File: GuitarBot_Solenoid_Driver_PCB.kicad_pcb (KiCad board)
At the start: 2 copper layers, 68 parts, among them J3V3 Screw_Terminal_01x02, Q1 NMOS, Q10 NMOS, Q11 NMOS, Q12 NMOS, Q13 NMOS, Q14 NMOS, Q15 NMOS, Q16 NMOS, Q2 NMOS, Q3 NMOS, Q4 NMOS, Q5 NMOS, Q6 NMOS, Q7 NMOS, Q8 NMOS, Q9 NMOS, U1 MCP23017_SP

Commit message: initial schematics for ilya rennovations
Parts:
- added C2: 1uF, Capacitor_THT:C_Radial_D10.0mm_H16.0mm_P5.00mm, F.Cu at (83.8, 55.9)
- added H1: MountingHole, MountingHole:MountingHole_3.2mm_M3, F.Cu at (57.4, 41.9)
- added H2: MountingHole, MountingHole:MountingHole_3.2mm_M3, F.Cu at (59.3, 142.2)
- added H3: MountingHole, MountingHole:MountingHole_3.2mm_M3, F.Cu at (190.5, 142.2)
- added H4: MountingHole, MountingHole:MountingHole_3.2mm_M3, F.Cu at (190.5, 41.9)
- added R25: 100k, Resistor_THT:R_Axial_DIN0207_L6.3mm_D2.5mm_P7.62mm_Horizontal, F.Cu at (114.3, 138.0)
- added R26: 100k, Resistor_THT:R_Axial_DIN0207_L6.3mm_D2.5mm_P7.62mm_Horizontal, F.Cu at (114.3, 131.6)
- added R27: 100k, Resistor_THT:R_Axial_DIN0207_L6.3mm_D2.5mm_P7.62mm_Horizontal, F.Cu at (114.3, 125.1)
- added R28: 100k, Resistor_THT:R_Axial_DIN0207_L6.3mm_D2.5mm_P7.62mm_Horizontal, F.Cu at (114.3, 118.7)
- added R29: 100k, Resistor_THT:R_Axial_DIN0207_L6.3mm_D2.5mm_P7.62mm_Horizontal, F.Cu at (114.3, 112.3)
- added R30: 100k, Resistor_THT:R_Axial_DIN0207_L6.3mm_D2.5mm_P7.62mm_Horizontal, F.Cu at (114.3, 105.8)
- added R31: 100k, Resistor_THT:R_Axial_DIN0207_L6.3mm_D2.5mm_P7.62mm_Horizontal, F.Cu at (114.3, 99.4)
- added R32: 100k, Resistor_THT:R_Axial_DIN0207_L6.3mm_D2.5mm_P7.62mm_Horizontal, F.Cu at (114.3, 93.0)
- added R33: 100k, Resistor_THT:R_Axial_DIN0207_L6.3mm_D2.5mm_P7.62mm_Horizontal, F.Cu at (114.3, 86.5)
- added R34: 100k, Resistor_THT:R_Axial_DIN0207_L6.3mm_D2.5mm_P7.62mm_Horizontal, F.Cu at (114.3, 80.1)
- added R35: 100k, Resistor_THT:R_Axial_DIN0207_L6.3mm_D2.5mm_P7.62mm_Horizontal, F.Cu at (114.3, 73.7)
- added R36: 100k, Resistor_THT:R_Axial_DIN0207_L6.3mm_D2.5mm_P7.62mm_Horizontal, F.Cu at (114.3, 67.2)
- added R37: 100k, Resistor_THT:R_Axial_DIN0207_L6.3mm_D2.5mm_P7.62mm_Horizontal, F.Cu at (114.3, 60.8)
- added R38: 100k, Resistor_THT:R_Axial_DIN0207_L6.3mm_D2.5mm_P7.62mm_Horizontal, F.Cu at (114.3, 54.4)
- added R39: 100k, Resistor_THT:R_Axial_DIN0207_L6.3mm_D2.5mm_P7.62mm_Horizontal, F.Cu at (114.3, 47.9)
- added R40: 100k, Resistor_THT:R_Axial_DIN0207_L6.3mm_D2.5mm_P7.62mm_Horizontal, F.Cu at (114.3, 41.5)
- C1: value 0.1uF -> 1000uF; footprint Capacitor_THT:C_Disc_D5.0mm_W2.5mm_P5.00mm -> Capacitor_THT:CP_Radial_D10.0mm_P5.00mm
- Q1, Q10, Q11, Q12, Q13, Q14, Q15, Q16, Q2, Q3, Q4, Q5, Q6, Q7, Q8, Q9: footprint Package_TO_SOT_THT:TO-220-3_Vertical -> Package_TO_SOT_THT:TO-251-3_Vertical
- R1, R2: value 4k8 -> 4k7
- R10, R11, R12, R13, R14, R15, R16, R17, R18, R19, R20, R21, R22, R23, R24, R9: value 100k -> 100
- moved R8 25.7 mm to (82.5, 115.6), turned to 90 degrees
- moved R6 21.9 mm to (72.4, 108.0), turned to -90 degrees
- moved R7 18.4 mm to (77.5, 115.6), turned to 90 degrees
- moved R5 14.6 mm to (67.3, 108.0), turned to -90 degrees
- moved Q1 12.7 mm to (117.3, 141.4)
- moved Q2 12.7 mm to (117.3, 135.0)
- moved Q3 12.7 mm to (117.3, 128.5)
- moved Q4 12.6 mm to (117.3, 122.1)
- moved Q5 12.6 mm to (117.3, 115.7)
- moved Q6 12.6 mm to (117.3, 109.2)
- moved Q7 12.6 mm to (117.3, 102.8)
- moved Q8 12.5 mm to (117.3, 96.3)
- moved Q16 12.5 mm to (117.3, 44.8)
- moved Q15 12.5 mm to (117.3, 51.2)
- moved Q14 12.4 mm to (117.3, 57.7)
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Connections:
- Q1 pad 1: /Sol1 -> /SOL_GATE1
- Q10 pad 1: /Sol10 -> /SOL_GATE10
- Q11 pad 1: /Sol11 -> /SOL_GATE11
- Q12 pad 1: /Sol12 -> /SOL_GATE12
- Q13 pad 1: /Sol13 -> /SOL_GATE13
- Q14 pad 1: /Sol14 -> /SOL_GATE14
- Q15 pad 1: /Sol15 -> /SOL_GATE15
- Q16 pad 1: /Sol16 -> /SOL_GATE16
- Q2 pad 1: /Sol2 -> /SOL_GATE2
- Q3 pad 1: /Sol3 -> /SOL_GATE3
- Q4 pad 1: /Sol4 -> /SOL_GATE4
- Q5 pad 1: /Sol5 -> /SOL_GATE5
- Q6 pad 1: /Sol6 -> /SOL_GATE6
- Q7 pad 1: /Sol7 -> /SOL_GATE7
- Q8 pad 1: /Sol8 -> /SOL_GATE8
- Q9 pad 1: /Sol9 -> /SOL_GATE9
- R10 pad 1: GNDPWR -> /SOL_GATE2
- R10 pad 2: /Sol2 -> Net-(U1-GPA1)
- R11 pad 1: GNDPWR -> /SOL_GATE3
- R11 pad 2: /Sol3 -> Net-(U1-GPA2)
- R12 pad 1: GNDPWR -> /SOL_GATE4
- R12 pad 2: /Sol4 -> Net-(U1-GPA3)
- R13 pad 1: GNDPWR -> /SOL_GATE5
- R13 pad 2: /Sol5 -> Net-(U1-GPA4)
- R14 pad 1: GNDPWR -> /SOL_GATE6
- R14 pad 2: /Sol6 -> Net-(U1-GPA5)
- R15 pad 1: GNDPWR -> /SOL_GATE7
- R15 pad 2: /Sol7 -> Net-(U1-GPA6)
- R16 pad 1: GNDPWR -> /SOL_GATE8
- R16 pad 2: /Sol8 -> Net-(U1-GPA7)
- R17 pad 1: GNDPWR -> /SOL_GATE9
- R17 pad 2: /Sol9 -> Net-(U1-GPB0)
- R18 pad 1: GNDPWR -> /SOL_GATE10
- R18 pad 2: /Sol10 -> Net-(U1-GPB1)
- R19 pad 1: GNDPWR -> /SOL_GATE11
- R19 pad 2: /Sol11 -> Net-(U1-GPB2)
- R20 pad 1: GNDPWR -> /SOL_GATE12
- R20 pad 2: /Sol12 -> Net-(U1-GPB3)
- R21 pad 1: GNDPWR -> /SOL_GATE13
- R21 pad 2: /Sol13 -> Net-(U1-GPB4)
- R22 pad 1: GNDPWR -> /SOL_GATE14
- R22 pad 2: /Sol14 -> Net-(U1-GPB5)
- R23 pad 1: GNDPWR -> /SOL_GATE15
- R23 pad 2: /Sol15 -> Net-(U1-GPB6)
- R24 pad 1: GNDPWR -> /SOL_GATE16
- R24 pad 2: /Sol16 -> Net-(U1-GPB7)
- R9 pad 1: GNDPWR -> /SOL_GATE1
- R9 pad 2: /Sol1 -> Net-(U1-GPA0)
- U1 pad 1: /Sol9 -> Net-(U1-GPB0)
- U1 pad 2: /Sol10 -> Net-(U1-GPB1)
- U1 pad 21: /Sol1 -> Net-(U1-GPA0)
- U1 pad 22: /Sol2 -> Net-(U1-GPA1)
- U1 pad 23: /Sol3 -> Net-(U1-GPA2)
- U1 pad 24: /Sol4 -> Net-(U1-GPA3)
- U1 pad 25: /Sol5 -> Net-(U1-GPA4)
- U1 pad 26: /Sol6 -> Net-(U1-GPA5)
- U1 pad 27: /Sol7 -> Net-(U1-GPA6)
- U1 pad 28: /Sol8 -> Net-(U1-GPA7)
- U1 pad 3: /Sol11 -> Net-(U1-GPB2)
- U1 pad 4: /Sol12 -> Net-(U1-GPB3)
- U1 pad 5: /Sol13 -> Net-(U1-GPB4)
- U1 pad 6: /Sol14 -> Net-(U1-GPB5)
- U1 pad 7: /Sol15 -> Net-(U1-GPB6)
- U1 pad 8: /Sol16 -> Net-(U1-GPB7)
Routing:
- net GNDPWR: track 378.6 -> 0.00 mm
- net +12V: track 178.6 -> 0.00 mm
- net Net-(D2-A): track 71.3 -> 0.00 mm
- net Net-(D15-A): track 68.7 -> 0.00 mm
- net /Sol1: track 65.8 -> 0.00 mm
- net /Sol16: track 64.5 -> 0.00 mm
- net Net-(D1-A): track 62.7 -> 0.00 mm
- net Net-(D16-A): track 62.6 -> 0.00 mm
- net Net-(D3-A): track 62.0 -> 0.00 mm
- net Net-(D14-A): track 61.1 -> 0.00 mm
- net /Sol2: track 57.6 -> 0.00 mm
- net /Sol15: track 57.0 -> 0.00 mm
- net Net-(D4-A): track 54.8 -> 0.00 mm
- net +3.3V: track 104.5 -> 50.5 mm
- net Net-(D13-A): track 53.8 -> 0.00 mm
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
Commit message: Finished up the layout, it passes DRC but idk how good it looks
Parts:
- moved H3 23.0 mm to (167.5, 142.2)
- moved H4 23.0 mm to (167.5, 41.9)
- moved F1 17.9 mm to (158.2, 69.6)
- moved JSOL2 17.9 mm to (157.0, 113.0)
- moved JSOL_PWR1 17.9 mm to (159.9, 43.5)
- moved C1 17.9 mm to (160.6, 55.6)
- moved D1 14.0 mm to (148.6, 140.9)
- moved D10 14.0 mm to (148.6, 85.0)
- moved D11 14.0 mm to (148.6, 78.2)
- moved D12 14.0 mm to (148.6, 71.5)
- moved D13 14.0 mm to (148.6, 64.7)
- moved D14 14.0 mm to (148.6, 58.0)
- moved D15 14.0 mm to (148.6, 51.2)
- moved D16 14.0 mm to (148.6, 44.5)
- moved D2 14.0 mm to (148.6, 134.9)
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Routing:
- net Net-(D15-A): track 0.00 -> 59.4 mm
- net Net-(D2-A): track 0.00 -> 55.6 mm
- net Net-(U1-GPB7): track 0.00 -> 55.5 mm
- net Net-(U1-GPA0): track 0.00 -> 54.8 mm
- net Net-(D14-A): track 0.00 -> 51.3 mm
- net Net-(D3-A): track 0.00 -> 48.2 mm
- net Net-(U1-GPB6): track 0.00 -> 47.9 mm
- net Net-(U1-GPA1): track 0.00 -> 46.7 mm
- net Net-(D16-A): track 0.00 -> 45.4 mm
- net +3.3V: track 50.5 -> 5.19 mm
- net Net-(D13-A): track 0.00 -> 43.1 mm
- net Net-(D1-A): track 0.00 -> 43.1 mm
- net Net-(D4-A): track 0.00 -> 40.8 mm
- net Net-(U1-GPB5): track 0.00 -> 40.4 mm
- net Net-(U1-GPA2): track 0.00 -> 38.7 mm
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- added copper zone on F.Cu, net +12V
- added copper zone on F.Cu, net +3.3V
- added copper zone on B.Cu, net GNDPWR
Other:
- board outline added: 123.7 x 114.2 mm
- board text removed: "${REFERENCE}"

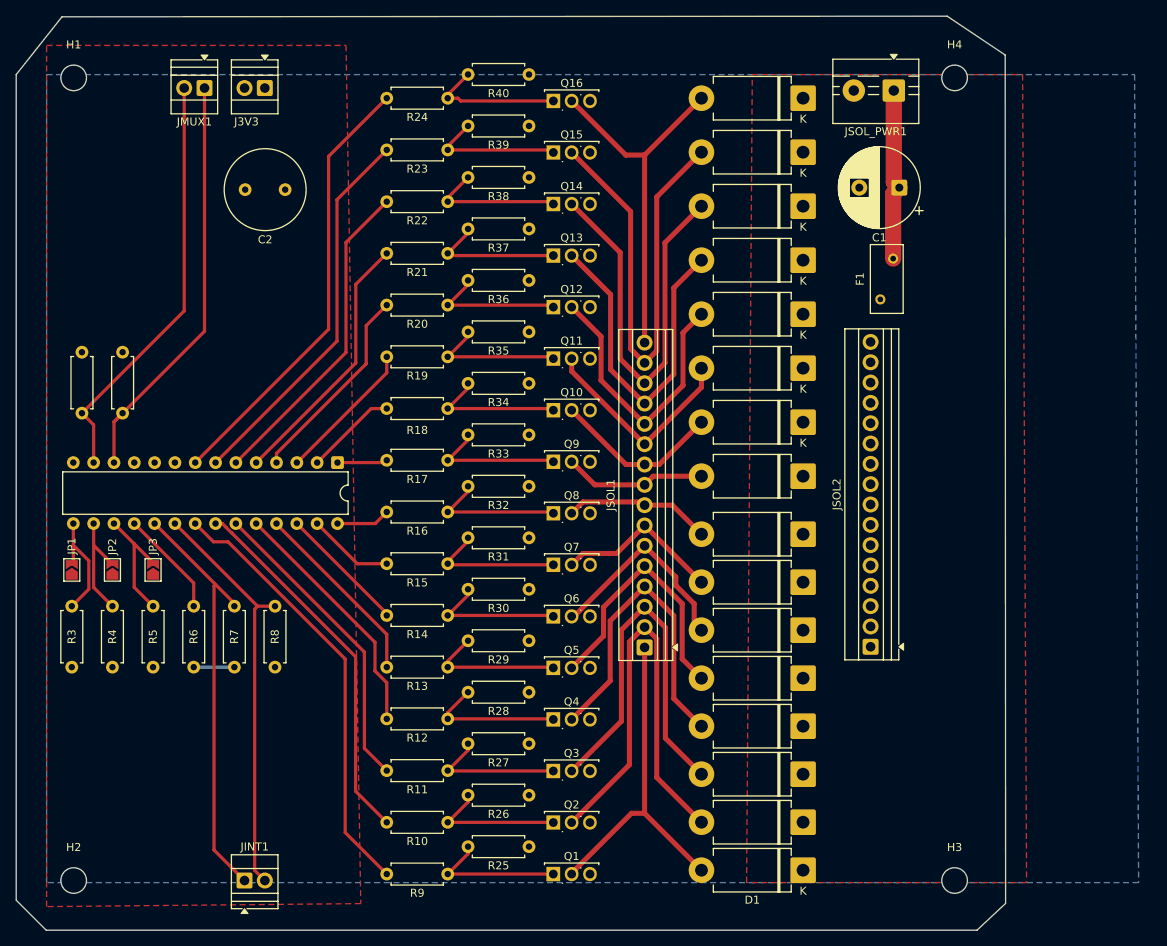
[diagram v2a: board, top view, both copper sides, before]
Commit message: Fixed connectection issue with resistors
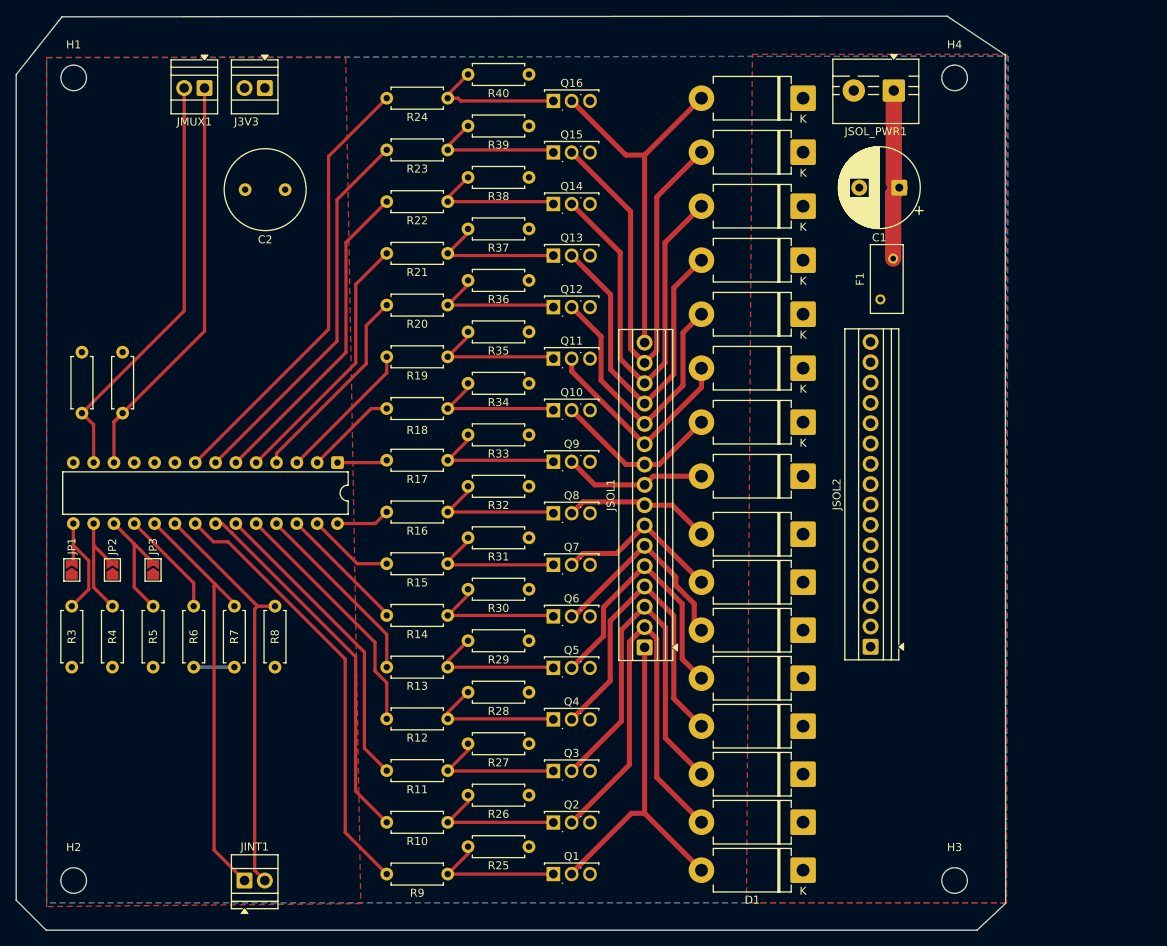
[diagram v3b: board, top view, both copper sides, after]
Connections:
- R33 pad 1: unconnected-(R33-Pad1) -> GNDPWR
- R34 pad 1: unconnected-(R34-Pad1) -> GNDPWR
- R35 pad 1: unconnected-(R35-Pad1) -> GNDPWR
- R36 pad 1: unconnected-(R36-Pad1) -> GNDPWR
- R37 pad 1: unconnected-(R37-Pad1) -> GNDPWR
- R38 pad 1: unconnected-(R38-Pad1) -> GNDPWR
- R39 pad 1: unconnected-(R39-Pad1) -> GNDPWR
- R40 pad 1: unconnected-(R40-Pad1) -> GNDPWR
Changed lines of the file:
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@@
 	(net 61 "Net-(U1-GPA6)")
 	(net 62 "Net-(U1-GPA7)")
-	(net 63 "unconnected-(R33-Pad1)")
-	(net 64 "unconnected-(R34-Pad1)")
-	(net 65 "unconnected-(R35-Pad1)")
-	(net 66 "unconnected-(R36-Pad1)")
-	(net 67 "unconnected-(R37-Pad1)")
-	(net 68 "unconnected-(R38-Pad1)")
-	(net 69 "unconnected-(R39-Pad1)")
-	(net 70 "unconnected-(R40-Pad1)")
 	(footprint "Resistor_THT:R_Axial_DIN0207_L6.3mm_D2.5mm_P7.62mm_Horizontal"
 		(layer "F.Cu")
@@
 			(layers "*.Cu" "*.Mask")
 			(remove_unused_layers no)
-			(net 63 "unconnected-(R33-Pad1)")
+			(net 2 "GNDPWR")
 			(pintype "passive")
 		)
@@
 			(layers "*.Cu" "*.Mask")
 			(remove_unused_layers no)
-			(net 64 "unconnected-(R34-Pad1)")
+			(net 2 "GNDPWR")
 			(pintype "passive")
 		)
@@
 			(layers "*.Cu" "*.Mask")
 			(remove_unused_layers no)
-			(net 66 "unconnected-(R36-Pad1)")
+			(net 2 "GNDPWR")
 			(pintype "passive")
 		)
@@
 			(layers "*.Cu" "*.Mask")
 			(remove_unused_layers no)
-			(net 68 "unconnected-(R38-Pad1)")
+			(net 2 "GNDPWR")
 			(pintype "passive")
 		)
@@
 			(layers "*.Cu" "*.Mask")
 			(remove_unused_layers no)
-			(net 70 "unconnected-(R40-Pad1)")
+			(net 2 "GNDPWR")
 			(pintype "passive")
 		)
@@
 			(layers "*.Cu" "*.Mask")
 			(remove_unused_layers no)
-			(net 69 "unconnected-(R39-Pad1)")
+			(net 2 "GNDPWR")
 			(pintype "passive")
 		)
@@
 		(sheetname "/")
 		(sheetfile "GuitarBot_Solenoid_Driver_PCB.kicad_sch")
+		(attr exclude_from_bom)
 		(fp_circle
 			(center 0 0)
@@
 			(layers "*.Cu" "*.Mask")
 			(remove_unused_layers no)
-			(net 65 "unconnected-(R35-Pad1)")
+			(net 2 "GNDPWR")
 			(pintype "passive")
 		)
@@
 			(layers "*.Cu" "*.Mask")
 			(remove_unused_layers no)
-			(net 67 "unconnected-(R37-Pad1)")
+			(net 2 "GNDPWR")
 			(pintype "passive")
 		)
@@
 		(polygon
 			(pts
-				(xy 176 41.5) (xy 176.5 142.5) (xy 141.5 142.5) (xy 142.21 41.5)
+				(xy 173.99 38.96) (xy 173.99 145.04) (xy 141.482145 145.04) (xy 142.227855 38.96)
 			)
 		)
@@
 		(polygon
 			(pts
-				(xy 54 37.85) (xy 91.427723 37.85) (xy 93.275 145.125) (xy 54 145.5)
+				(xy 54 39.37) (xy 91.382264 39.37) (xy 93.275 145.125) (xy 54 145.5)
 			)
 		)
@@
 		(polygon
 			(pts
-				(xy 54 41.5) (xy 190 41.5) (xy 190.5 142.5) (xy 54 142.5)
+				(xy 54 39.37) (xy 174.184231 39.175769) (xy 173.985225 145.04) (xy 54 145.04)
 			)
 		)

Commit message: changed 01x16 terminal blocks from 2.54mm to 5.08mm
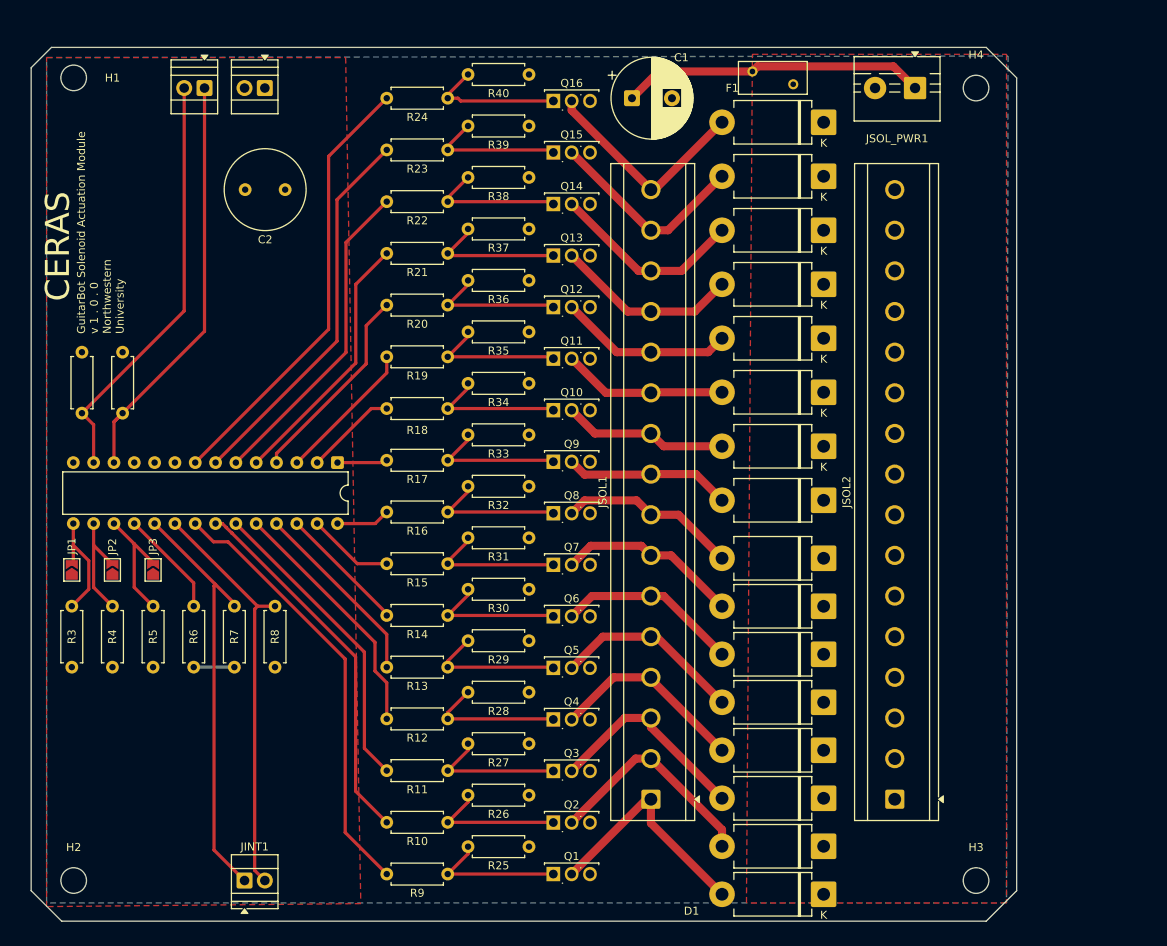
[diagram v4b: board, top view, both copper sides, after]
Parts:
- JSOL1, JSOL2: footprint TerminalBlock:TerminalBlock_Xinya_XY308-2.54-16P_1x16_P2.54mm_Horizontal -> TerminalBlock_CUI:TerminalBlock_CUI_TB007-508-16_1x16_P5.08mm_Horizontal
- moved C1 35.2 mm to (127.2, 44.5), turned to 0 degrees
- moved F1 29.0 mm to (147.3, 42.7), turned to 180 degrees
- moved JSOL2 19.3 mm to (160.0, 132.1)
- moved JSOL1 19.0 mm to (129.5, 132.1)
- moved D1 3.96 mm to (151.1, 144.0)
- moved D2 3.96 mm to (151.1, 138.0)
- moved D3 3.96 mm to (151.1, 132.0)
- moved D14 3.96 mm to (151.1, 61.0)
- moved D15 3.96 mm to (151.1, 54.2)
- moved D16 3.96 mm to (151.1, 47.5)
- moved D10 3.96 mm to (151.1, 88.0)
- moved D11 3.96 mm to (151.1, 81.2)
- moved D12 3.96 mm to (151.1, 74.5)
- moved D13 3.96 mm to (151.1, 67.7)
- moved D4 3.96 mm to (151.1, 126.0)
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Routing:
- net Net-(D15-A): track 59.4 -> 25.6 mm
- net Net-(D2-A): track 55.6 -> 27.9 mm
- net Net-(D14-A): track 51.3 -> 24.4 mm
- net Net-(D3-A): track 48.2 -> 26.4 mm
- net Net-(D13-A): track 43.1 -> 23.1 mm
- net Net-(D16-A): track 45.4 -> 27.6 mm
- net Net-(JSOL_PWR1-Pin_1): track 21.6 -> 38.2 mm
- net Net-(D4-A): track 40.8 -> 24.9 mm
- net Net-(D1-A): track 43.1 -> 29.3 mm
- net Net-(D12-A): track 35.5 -> 21.9 mm
- net Net-(D5-A): track 33.5 -> 23.8 mm
- net Net-(D11-A): track 26.9 -> 20.6 mm
- net Net-(D8-A): track 18.5 -> 22.5 mm
- net Net-(D6-A): track 26.3 -> 22.9 mm
- net Net-(D9-A): track 17.9 -> 20.8 mm
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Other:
- board size 123.7 x 114.2 mm -> 123.2 x 109.2 mm
- board text added: "CERAS"
- board text added: "GuitarBot Solenoid Actuation Module v 1 . 0 . 0 Northwestern University"

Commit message: Minimal changes to naming
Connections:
- net /SDK renamed /SCK
